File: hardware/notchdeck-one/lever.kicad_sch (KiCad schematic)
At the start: 50 parts, among them J10 POWER MAG, J11 BRAKE MAG, J12 POWER S0, J13 POWER S1, J14 POWER S2, J5 BRAKE S0, J6 BRAKE S1, J7 BRAKE S2, J8 BRAKE S3, U10 USBLC6-2SC6, U11 USBLC6-2SC6, U5 AS5600, U9 TCA9543APWR

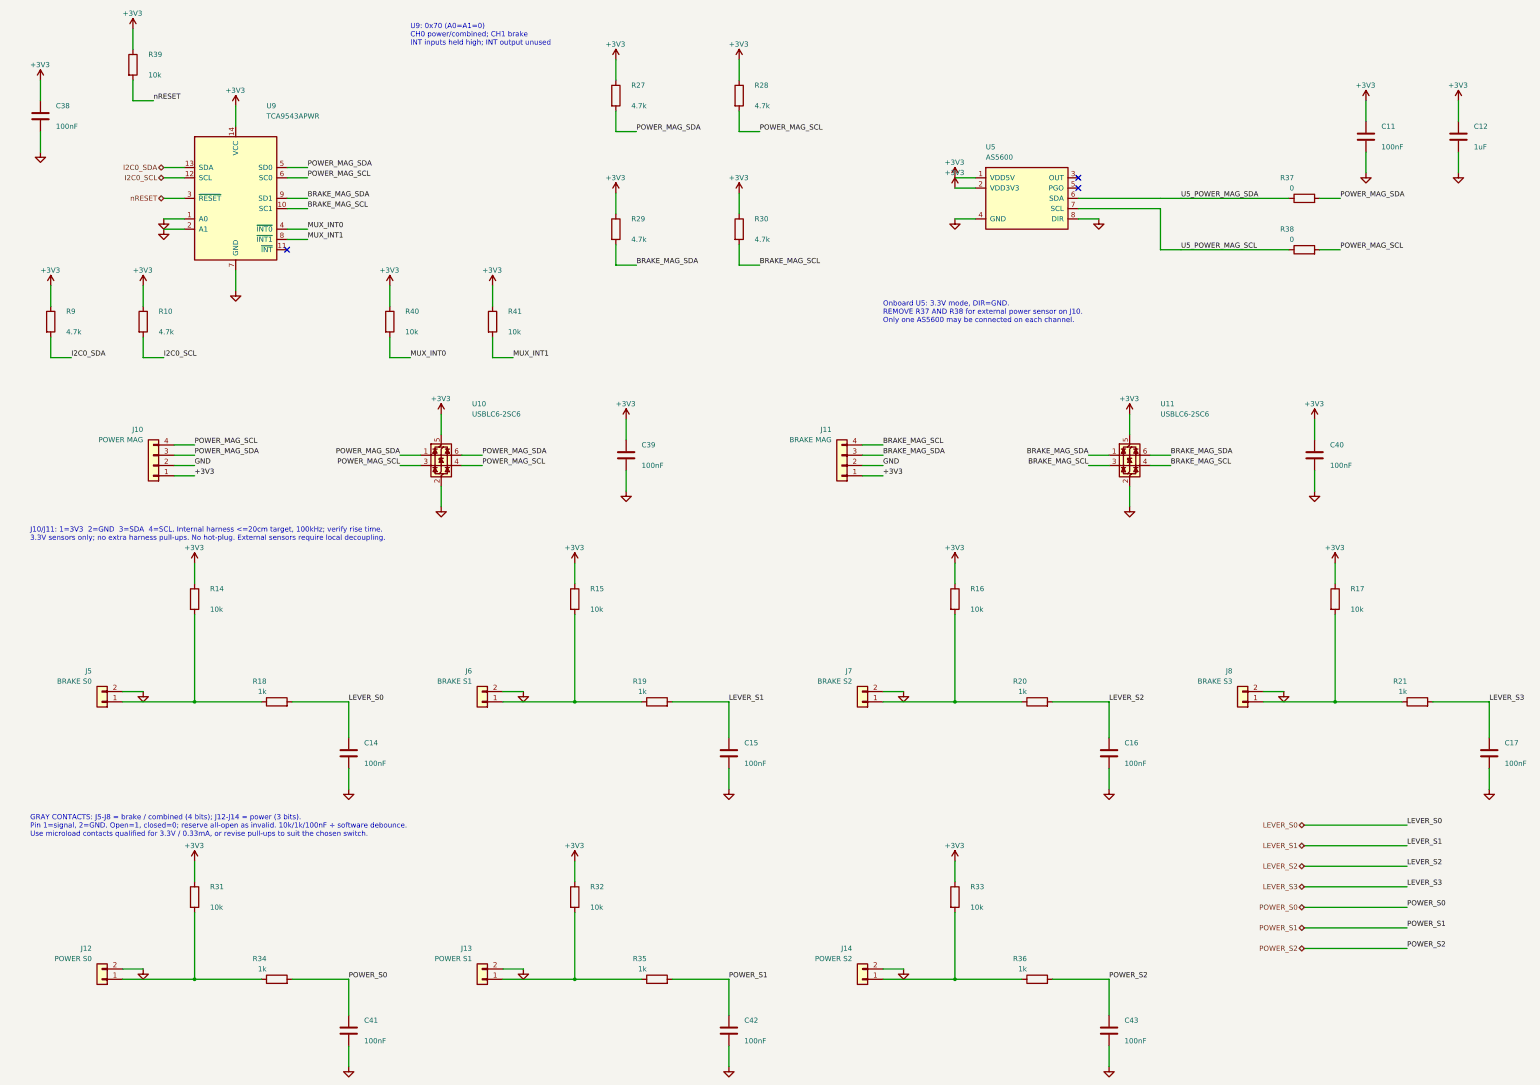
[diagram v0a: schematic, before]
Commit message: Add keyed harnesses and build plan for Japanese-style dual and mascon handles
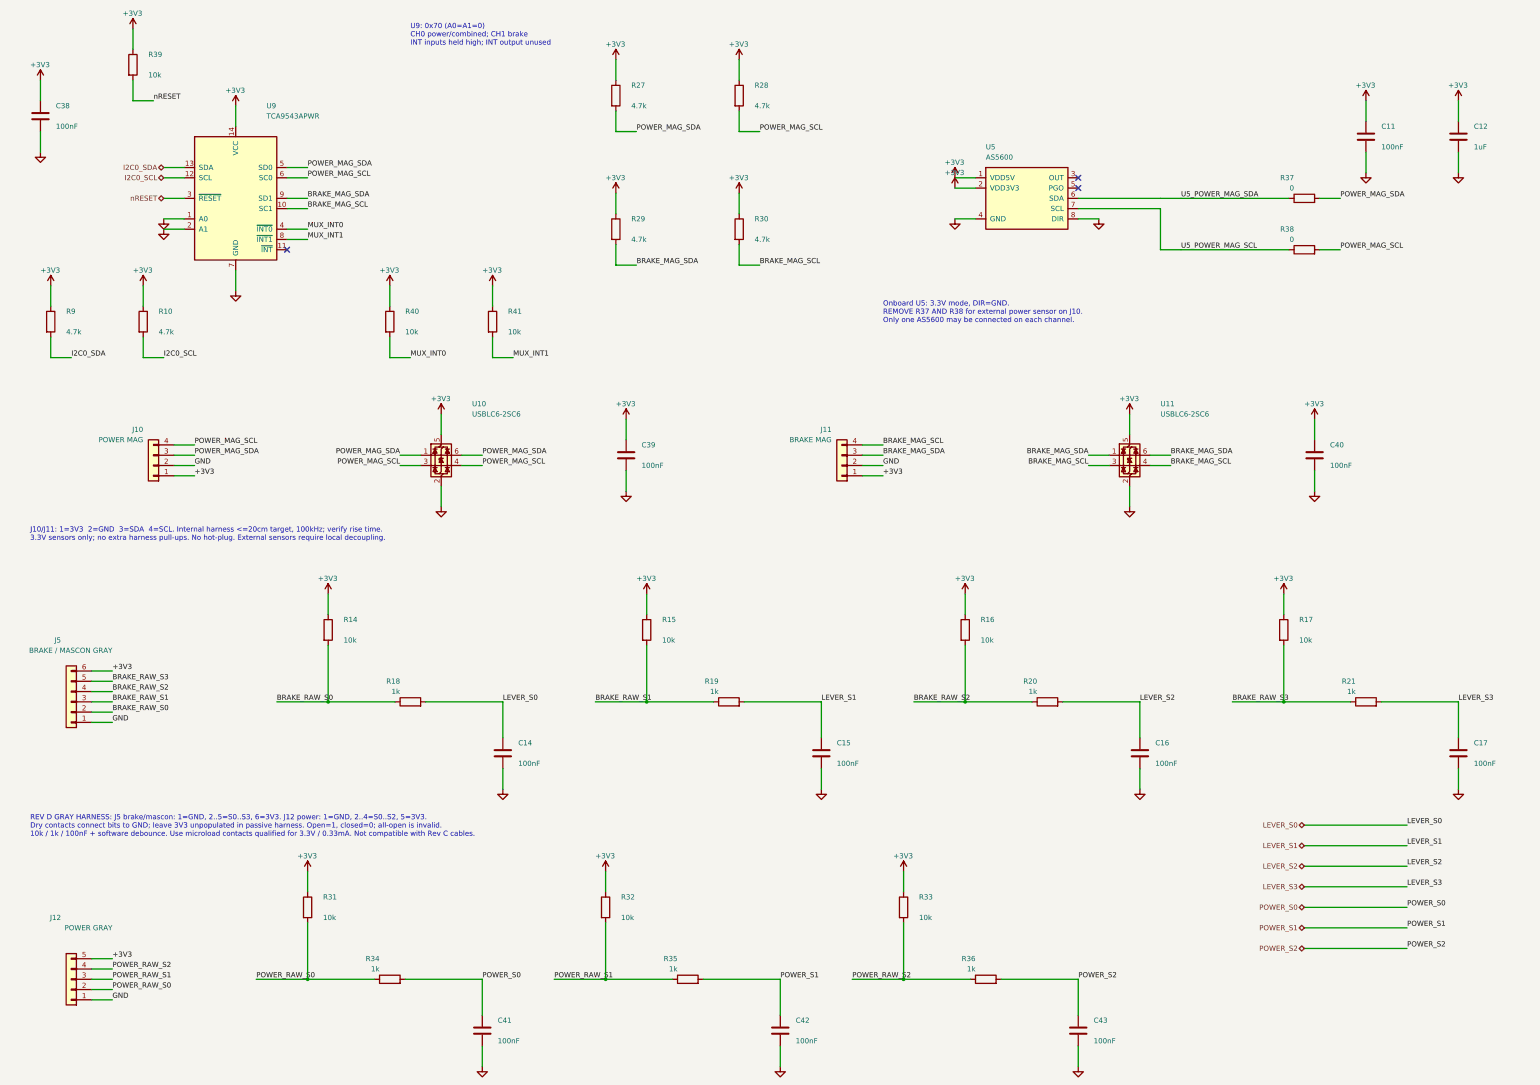
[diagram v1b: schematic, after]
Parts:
- removed J13: POWER S1, Connector_JST:JST_PH_S2B-PH-SM4-TB_1x02-1MP_P2.00mm_Horizontal, symbol Connector_Generic:Conn_01x02
- removed J14: POWER S2, Connector_JST:JST_PH_S2B-PH-SM4-TB_1x02-1MP_P2.00mm_Horizontal, symbol Connector_Generic:Conn_01x02
- removed J6: BRAKE S1, Connector_JST:JST_PH_S2B-PH-SM4-TB_1x02-1MP_P2.00mm_Horizontal, symbol Connector_Generic:Conn_01x02
- removed J7: BRAKE S2, Connector_JST:JST_PH_S2B-PH-SM4-TB_1x02-1MP_P2.00mm_Horizontal, symbol Connector_Generic:Conn_01x02
- removed J8: BRAKE S3, Connector_JST:JST_PH_S2B-PH-SM4-TB_1x02-1MP_P2.00mm_Horizontal, symbol Connector_Generic:Conn_01x02
- J12: value POWER S0 -> POWER GRAY; footprint Connector_JST:JST_PH_S2B-PH-SM4-TB_1x02-1MP_P2.00mm_Horizontal -> Connector_JST:JST_PH_S5B-PH-SM4-TB_1x05-1MP_P2.00mm_Horizontal; symbol Connector_Generic:Conn_01x02 -> Connector_Generic:Conn_01x05; BOM Comments Mating harnesses not included. J2: protected 1S cell, pin 1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 -> Rev D power Gray harness: pin1=GND, pins2..4=S0..S2, pin5=3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; LCSC C295747 -> C265104; MPN S2B-PH-SM4-TB(LF)(SN) -> S5B-PH-SM4-TB(LF)(SN)
- J5: value BRAKE S0 -> BRAKE / MASCON GRAY; footprint Connector_JST:JST_PH_S2B-PH-SM4-TB_1x02-1MP_P2.00mm_Horizontal -> Connector_JST:JST_PH_S6B-PH-SM4-TB_1x06-1MP_P2.00mm_Horizontal; symbol Connector_Generic:Conn_01x02 -> Connector_Generic:Conn_01x06; BOM Comments Mating harnesses not included. J2: protected 1S cell, pin 1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 -> Rev D brake/mascon Gray harness: pin1=GND, pins2..5=S0..S3,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; LCSC C295747 -> C265405; MPN S2B-PH-SM4-TB(LF)(SN) -> S6B-PH-SM4-TB(LF)(SN)
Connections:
- net +3V3: now also J12.5 (Pin_5), J5.6 (Pin_6)
- net GND: now also J12.1 (Pin_1), J5.1 (Pin_1); no longer J12.2 (Pin_2), J5.2 (Pin_2)
- net BRAKE_RAW_S1: now reaches R15.2, R19.1
- net BRAKE_RAW_S1: now also J5.3 (Pin_3)
- net POWER_RAW_S0: now reaches R31.2, R34.1
- net POWER_RAW_S0: now also J12.2 (Pin_2); no longer J12.1 (Pin_1)
- net BRAKE_RAW_S0: now reaches R14.2, R18.1
- net BRAKE_RAW_S0: now also J5.2 (Pin_2); no longer J5.1 (Pin_1)
- net POWER_RAW_S1: now reaches R32.2, R35.1
- net POWER_RAW_S1: now also J12.3 (Pin_3)
- net POWER_RAW_S2: now reaches R33.2, R36.1
- net POWER_RAW_S2: now also J12.4 (Pin_4)
- net BRAKE_RAW_S3: now reaches R17.2, R21.1
- net BRAKE_RAW_S3: now also J5.5 (Pin_5)
- net BRAKE_RAW_S2: now reaches R16.2, R20.1
- net BRAKE_RAW_S2: now also J5.4 (Pin_4)
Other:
- note added: "REV D GRAY HARNESS: J5 brake/mascon: 1=GND, 2..5=S0..S3, 6=3V3. J12 power: 1=GND, 2..4=S0..S2, 5=3V3. Dry contacts connect bits to GND; leave 3V3 unpopulated in passive harness. Open=1, closed=0; all-open is invalid. 10k / 1k / 100nF + software debounce. Use microload contacts qualified for 3.3V / 0.33mA. Not compatible with Rev C cables."
- note removed: "GRAY CONTACTS: J5-J8 = brake / combined (4 bits); J12-J14 = power (3 bits). Pin 1=signal, 2=GND. Open=1, closed=0; reserve all-open as invalid. 10k/1k/100nF + software debounce. Use microload contacts qualified for 3.3V / 0.33mA, or revise pull-ups to suit the chosen switch."
- moved on the sheet: C14, C15, C16, C17, C41, C42, C43, R14, R15, R16, R17, R18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

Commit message: Add protected PWM actuator outputs and charger interlock
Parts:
- J10, J11: BOM Checked 2026-10-03 -> 2026-10-05
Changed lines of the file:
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@@
 	(title_block
 		(title "NotchDeck One — Power and brake handle interfaces")
-		(date "2026-10-03")
-		(rev "E")
+		(date "2026-10-04")
+		(rev "F")
 		(company "BenchBits")
 	)
@@
 			(effects (font (size 1.27 1.27))) (hide yes)
 		)
-		(property "BOM Checked" "2026-10-03"
+		(property "BOM Checked" "2026-10-05"
 			(at 50.8000 124.4600 0)
 			(effects (font (size 1.27 1.27))) (hide yes)
@@
 			(effects (font (size 1.27 1.27))) (hide yes)
 		)
-		(property "BOM Checked" "2026-10-03"
+		(property "BOM Checked" "2026-10-05"
 			(at 220.9800 124.4600 0)
 			(effects (font (size 1.27 1.27))) (hide yes)
